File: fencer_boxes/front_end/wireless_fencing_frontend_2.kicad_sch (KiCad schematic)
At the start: 19 parts, among them J1 Conn_01x03, J2 Conn_01x08, U2 AD8619

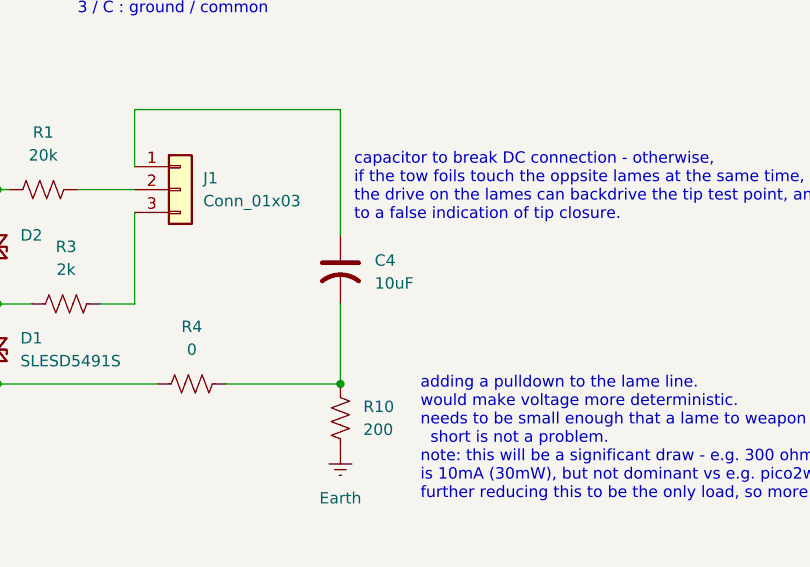
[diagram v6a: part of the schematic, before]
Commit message: change lame capacitor to 250 uF
seems to handle sweat etc better
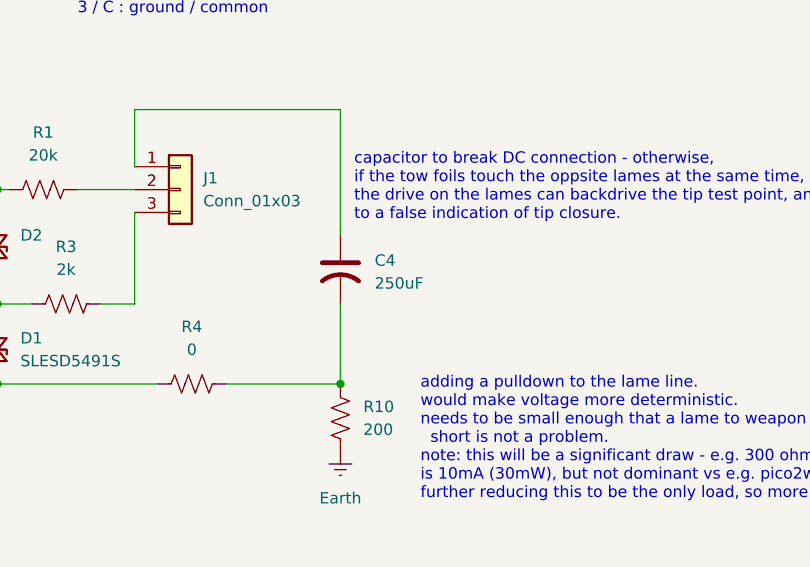
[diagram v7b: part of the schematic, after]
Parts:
- C4: value 10uF -> 250uF
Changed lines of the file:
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@@
 			)
 		)
-		(property "Value" "10uF"
+		(property "Value" "250uF"
 			(at 254 112.0139 0)
 			(effects
